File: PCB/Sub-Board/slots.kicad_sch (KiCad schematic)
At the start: 136 parts, among them J10 Type, J11 Power/I2C, J12 Address, J13 Power/I2C, J14 Address, J15 GPIO, J16 Type, J17 GPIO, J18 Type, J19 Power/I2C, J20 Address, J21 Power/I2C, J22 Address, J23 GPIO, J24 Type, J25 GPIO, J26 Type, J27 Power/I2C, J28 Address, J29 Power/I2C, J3 Power/I2C, J30 Address, J31 GPIO, J32 Type, J33 GPIO, J34 Type, J4 Address, J5 Power/I2C, J6 Address, J7 GPIO, J8 Type, J9 GPIO

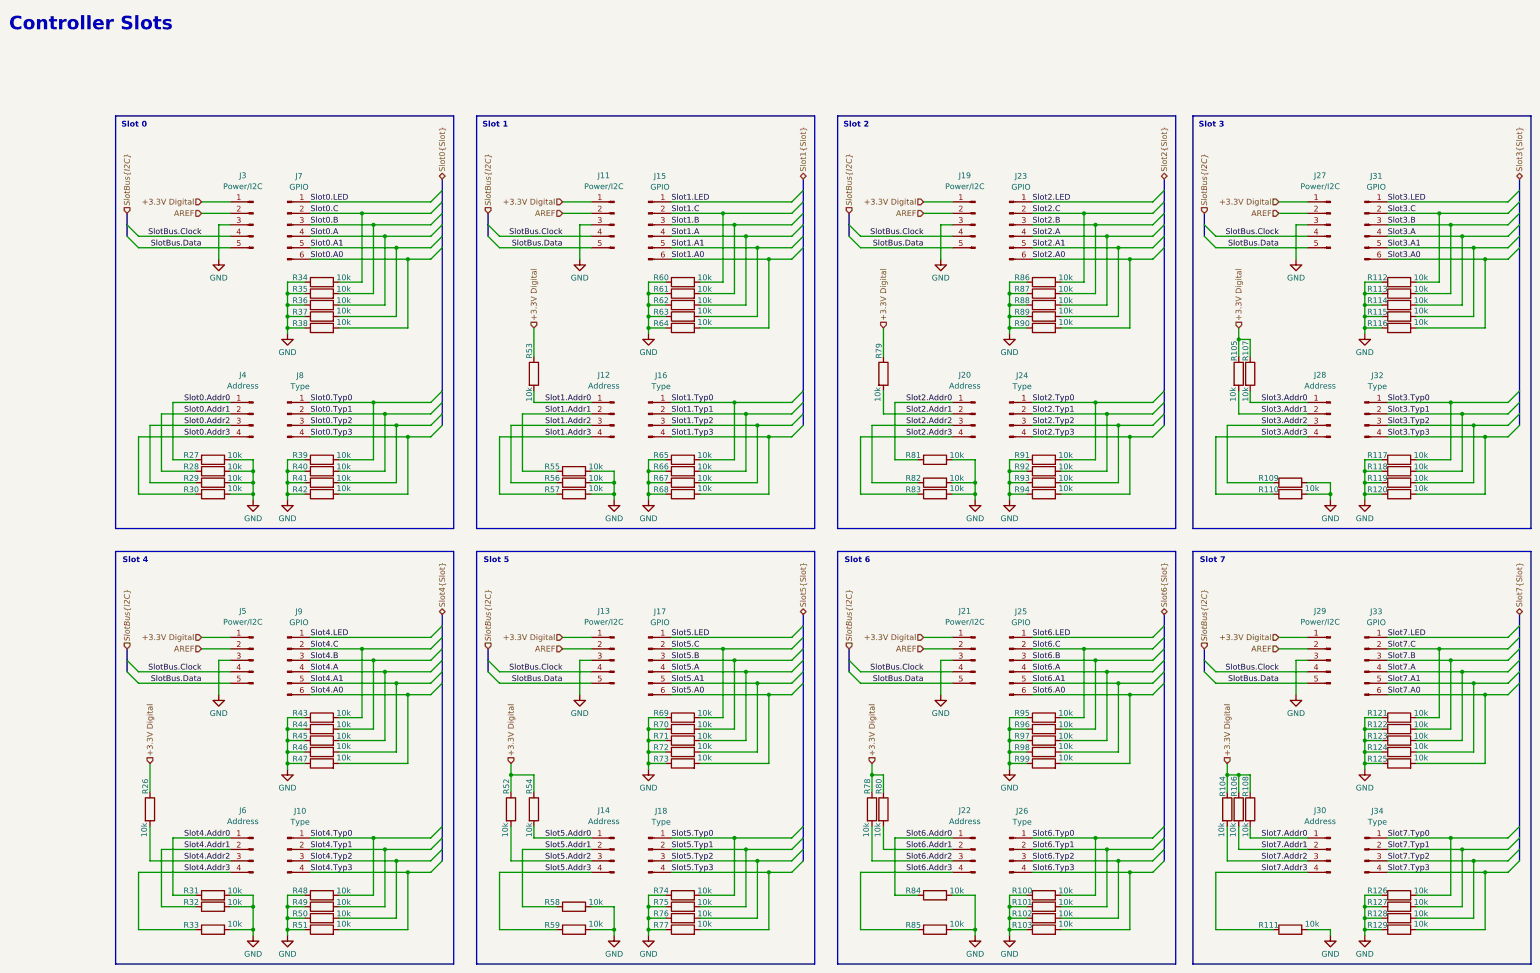
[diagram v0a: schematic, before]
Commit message: Sub Board PCB: Slot2 routing
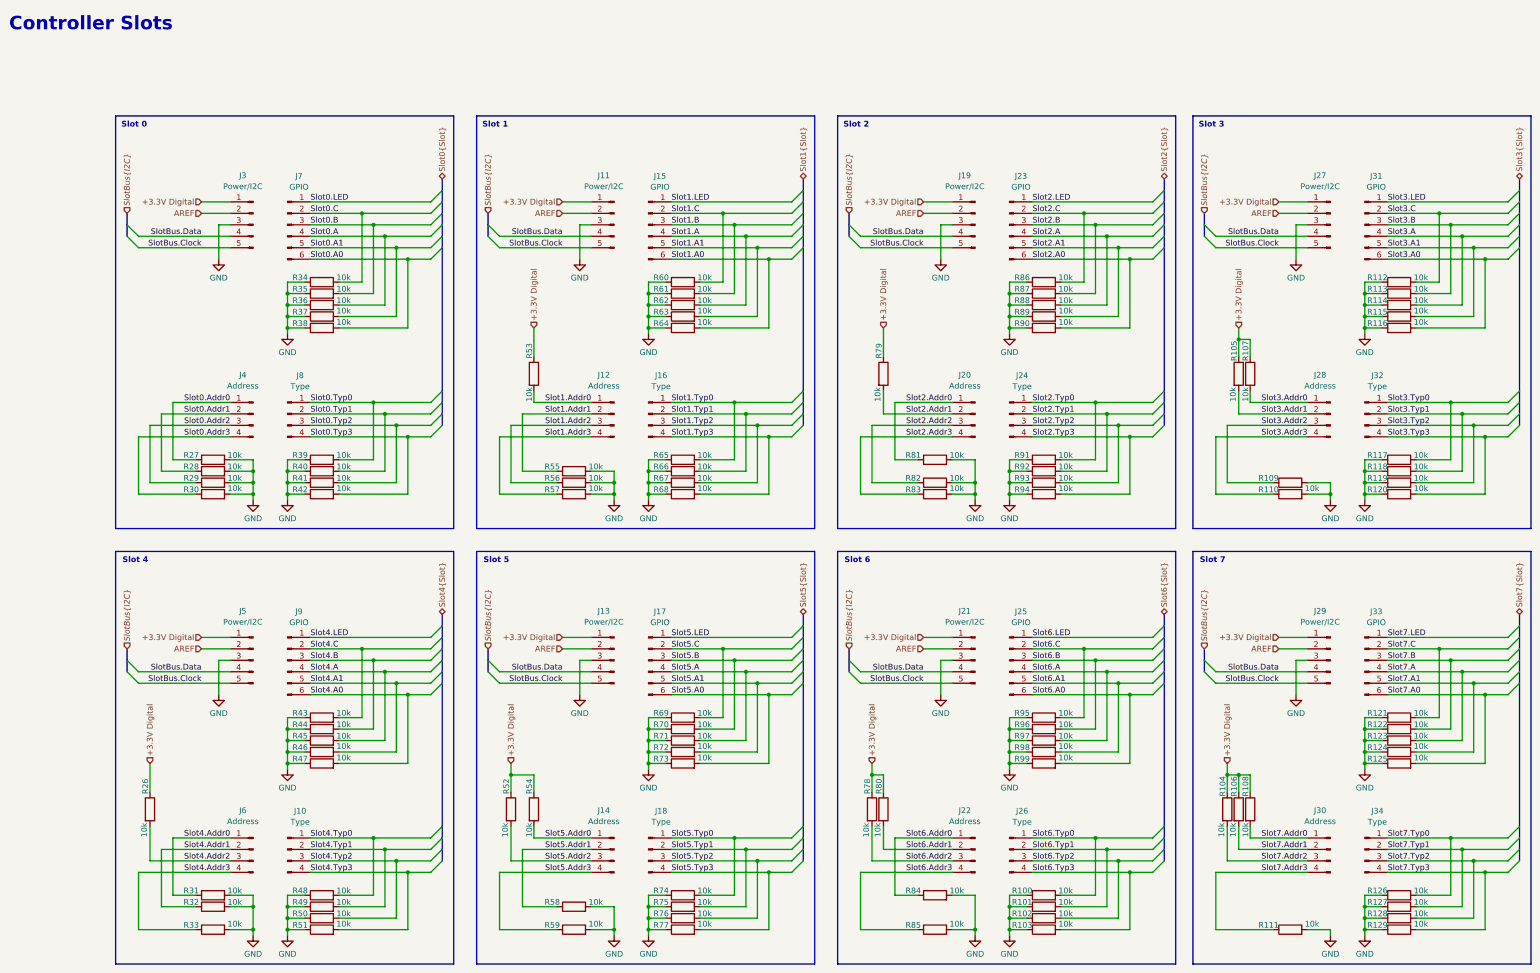
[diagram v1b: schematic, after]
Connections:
- net SlotBus.Clock: now also J11.5 (Pin_5), J13.5 (Pin_5), J19.5 (Pin_5), J21.5 (Pin_5), J27.5 (Pin_5), J29.5 (Pin_5), J3.5 (Pin_5), J5.5 (Pin_5); no longer J11.4 (Pin_4), J13.4 (Pin_4), J19.4 (Pin_4), J21.4 (Pin_4), J27.4 (Pin_4), J29.4 (Pin_4), J3.4 (Pin_4), J5.4 (Pin_4)
- net SlotBus.Data: now also J11.4 (Pin_4), J13.4 (Pin_4), J19.4 (Pin_4), J21.4 (Pin_4), J27.4 (Pin_4), J29.4 (Pin_4), J3.4 (Pin_4), J5.4 (Pin_4); no longer J11.5 (Pin_5), J13.5 (Pin_5), J19.5 (Pin_5), J21.5 (Pin_5), J27.5 (Pin_5), J29.5 (Pin_5), J3.5 (Pin_5), J5.5 (Pin_5)
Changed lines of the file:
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@@
 		)
 	)
-	(label "SlotBus.Data"
+	(label "SlotBus.Clock"
 		(at 149.86 173.99 180)
 		(effects
@@
 		)
 	)
-	(label "SlotBus.Clock"
+	(label "SlotBus.Data"
 		(at 149.86 74.93 180)
 		(effects
@@
 		)
 	)
-	(label "SlotBus.Clock"
+	(label "SlotBus.Data"
 		(at 229.87 74.93 180)
 		(effects
@@
 		)
 	)
-	(label "SlotBus.Clock"
+	(label "SlotBus.Data"
 		(at 308.61 171.45 180)
 		(effects
@@
 		)
 	)
-	(label "SlotBus.Clock"
+	(label "SlotBus.Data"
 		(at 69.85 171.45 180)
 		(effects
@@
 		)
 	)
-	(label "SlotBus.Data"
+	(label "SlotBus.Clock"
 		(at 69.85 77.47 180)
 		(effects
@@
 		)
 	)
-	(label "SlotBus.Data"
+	(label "SlotBus.Clock"
 		(at 229.87 77.47 180)
 		(effects
@@
 		)
 	)
-	(label "SlotBus.Data"
+	(label "SlotBus.Clock"
 		(at 229.87 173.99 180)
 		(effects
@@
 		)
 	)
-	(label "SlotBus.Clock"
+	(label "SlotBus.Data"
 		(at 308.61 74.93 180)
 		(effects
@@
 		)
 	)
-	(label "SlotBus.Clock"
+	(label "SlotBus.Data"
 		(at 69.85 74.93 180)
 		(effects
@@
 		)
 	)
-	(label "SlotBus.Data"
+	(label "SlotBus.Clock"
 		(at 149.86 77.47 180)
 		(effects
@@
 		)
 	)
-	(label "SlotBus.Data"
+	(label "SlotBus.Clock"
 		(at 69.85 173.99 180)
 		(effects
@@
 		)
 	)
-	(label "SlotBus.Data"
+	(label "SlotBus.Clock"
 		(at 308.61 173.99 180)
 		(effects
@@
 		)
 	)
-	(label "SlotBus.Clock"
+	(label "SlotBus.Data"
 		(at 149.86 171.45 180)
 		(effects
@@
 		)
 	)
-	(label "SlotBus.Data"
+	(label "SlotBus.Clock"
 		(at 308.61 77.47 180)
 		(effects
@@
 		)
 	)
-	(label "SlotBus.Clock"
+	(label "SlotBus.Data"
 		(at 229.87 171.45 180)
 		(effects
